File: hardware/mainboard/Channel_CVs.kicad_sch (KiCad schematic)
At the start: 44 parts, among them U901 MCP6004, U902 MCP6004

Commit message: hardware: resave files with KiCad v7.0.4
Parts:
- gave numbers to parts that had none: 42

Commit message: hardware: fix resistor value
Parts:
- R905, R911, R917, R923: value 480k -> 481k
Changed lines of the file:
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@@
 			)
 		)
-		(property "Value" "480k"
+		(property "Value" "481k"
 			(at 74.93 42.3164 90)
 			(effects
@@
 			)
 		)
-		(property "Value" "480k"
+		(property "Value" "481k"
 			(at 74.93 72.7964 90)
 			(effects
@@
 			)
 		)
-		(property "Value" "480k"
+		(property "Value" "481k"
 			(at 74.93 103.2764 90)
 			(effects
@@
 			)
 		)
-		(property "Value" "480k"
+		(property "Value" "481k"
 			(at 74.93 133.7564 90)
 			(effects

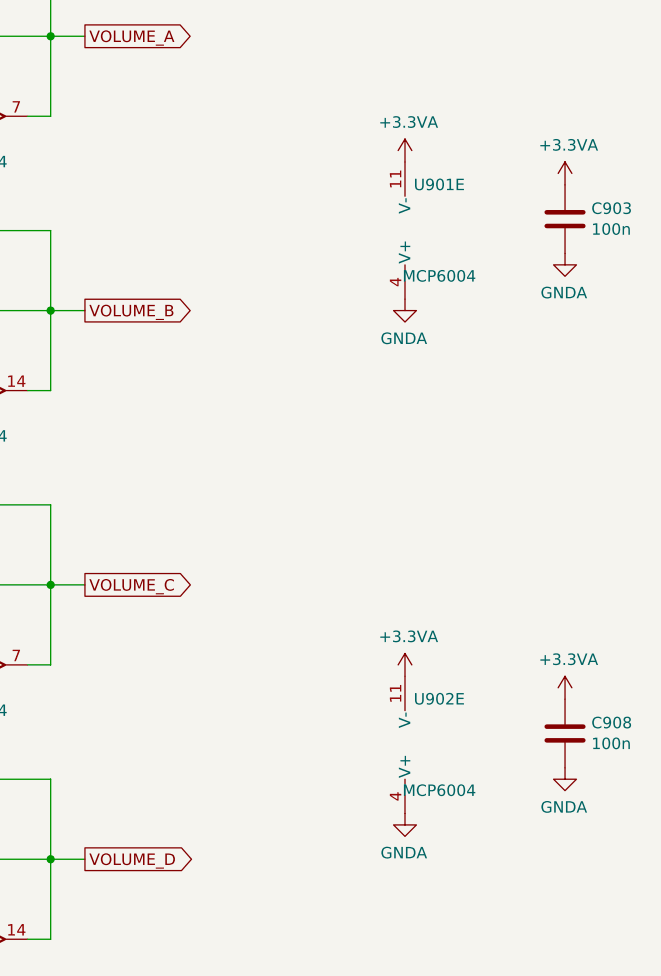
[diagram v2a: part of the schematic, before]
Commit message: hardware: fix reverse MCP6004 power pins
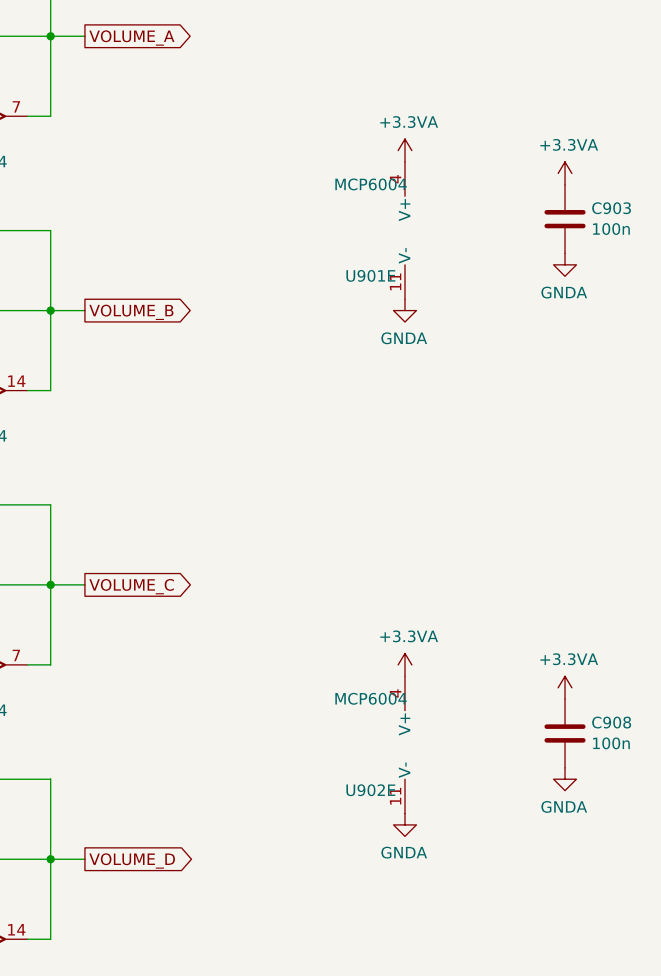
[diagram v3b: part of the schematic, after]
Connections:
- net +3.3VA: now also U901.4 (V+), U902.4 (V+); no longer U901.11 (V-), U902.11 (V-)
- net GNDA: now also U901.11 (V-), U902.11 (V-); no longer U901.4 (V+), U902.4 (V+)
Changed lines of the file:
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@@
 	(symbol
 		(lib_id "Amplifier_Operational:MCP6004")
-		(at 241.3 54.61 0)
-		(mirror x)
+		(at 236.22 54.61 0)
+		(mirror y)
 		(unit 5)
 		(exclude_from_sim no)
@@
 		(dnp no)
 		(property "Reference" "U901"
-			(at 242.57 49.53 0)
+			(at 234.95 59.69 0)
 			(effects
 				(font
@@
 		)
 		(property "Value" "MCP6004"
-			(at 242.57 59.69 0)
+			(at 234.95 49.53 0)
 			(effects
 				(font
@@
 		)
 		(property "Footprint" "Package_SO:SO-14_3.9x8.65mm_P1.27mm"
-			(at 240.03 57.15 0)
+			(at 237.49 52.07 0)
 			(effects
 				(font
@@
 		)
 		(property "Datasheet" "http://ww1.microchip.com/downloads/en/DeviceDoc/21733j.pdf"
-			(at 242.57 59.69 0)
-			(effects
-				(font
-					(size 1.27 1.27)
-				)
-				(hide yes)
-			)
-		)
-		(property "Description" ""
-			(at 241.3 54.61 0)
+			(at 234.95 49.53 0)
+			(effects
+				(font
+					(size 1.27 1.27)
+				)
+				(hide yes)
+			)
+		)
+		(property "Description" ""
+			(at 236.22 54.61 0)
 			(effects
 				(font
@@
 	(symbol
 		(lib_id "Amplifier_Operational:MCP6004")
-		(at 241.3 111.76 0)
-		(mirror x)
+		(at 236.22 111.76 0)
+		(mirror y)
 		(unit 5)
 		(exclude_from_sim no)
@@
 		(dnp no)
 		(property "Reference" "U902"
-			(at 242.57 106.68 0)
+			(at 234.95 116.84 0)
 			(effects
 				(font
@@
 		)
 		(property "Value" "MCP6004"
-			(at 242.57 116.84 0)
+			(at 234.95 106.68 0)
 			(effects
 				(font
@@
 		)
 		(property "Footprint" "Package_SO:SO-14_3.9x8.65mm_P1.27mm"
-			(at 240.03 114.3 0)
+			(at 237.49 109.22 0)
 			(effects
 				(font
@@
 		)
 		(property "Datasheet" "http://ww1.microchip.com/downloads/en/DeviceDoc/21733j.pdf"
-			(at 242.57 116.84 0)
-			(effects
-				(font
-					(size 1.27 1.27)
-				)
-				(hide yes)
-			)
-		)
-		(property "Description" ""
-			(at 241.3 111.76 0)
-			(effects
-				(font
+			(at 234.95 106.68 0)
+			(effects
+				(font
+					(size 1.27 1.27)
+				)
+				(hide yes)
+			)
+		)
+		(property "Description" ""
+			(at 236.22 111.76 0)
+			(effects
+				(font
